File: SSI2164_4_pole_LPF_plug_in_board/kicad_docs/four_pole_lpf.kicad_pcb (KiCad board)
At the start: 2 copper layers, 58.4 x 50.8 mm, 83 parts, among them J1 signal_in, J2 CV_in, J3 signal_out, J4 feedback_CV_and_power, Q1 MMBT3904, Q2 MMBT3906, Q3 BCM847DS135, Q4 MMBT3904, Q5 MMBT3904, Q6 MMBT3906, U1 SSM2164, U2 TL072, U3 TL072, U4 TL072, U5 TL072

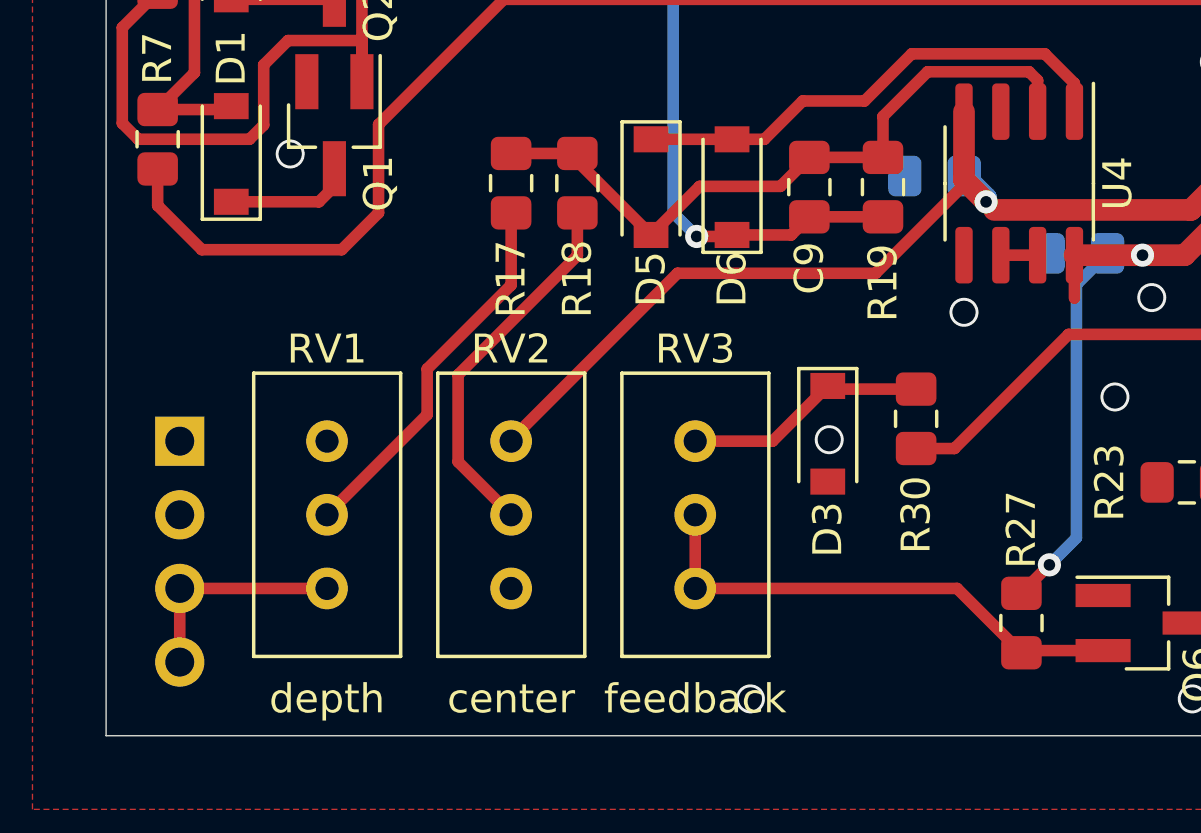
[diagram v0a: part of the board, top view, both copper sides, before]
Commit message: flip trimpots for consistency
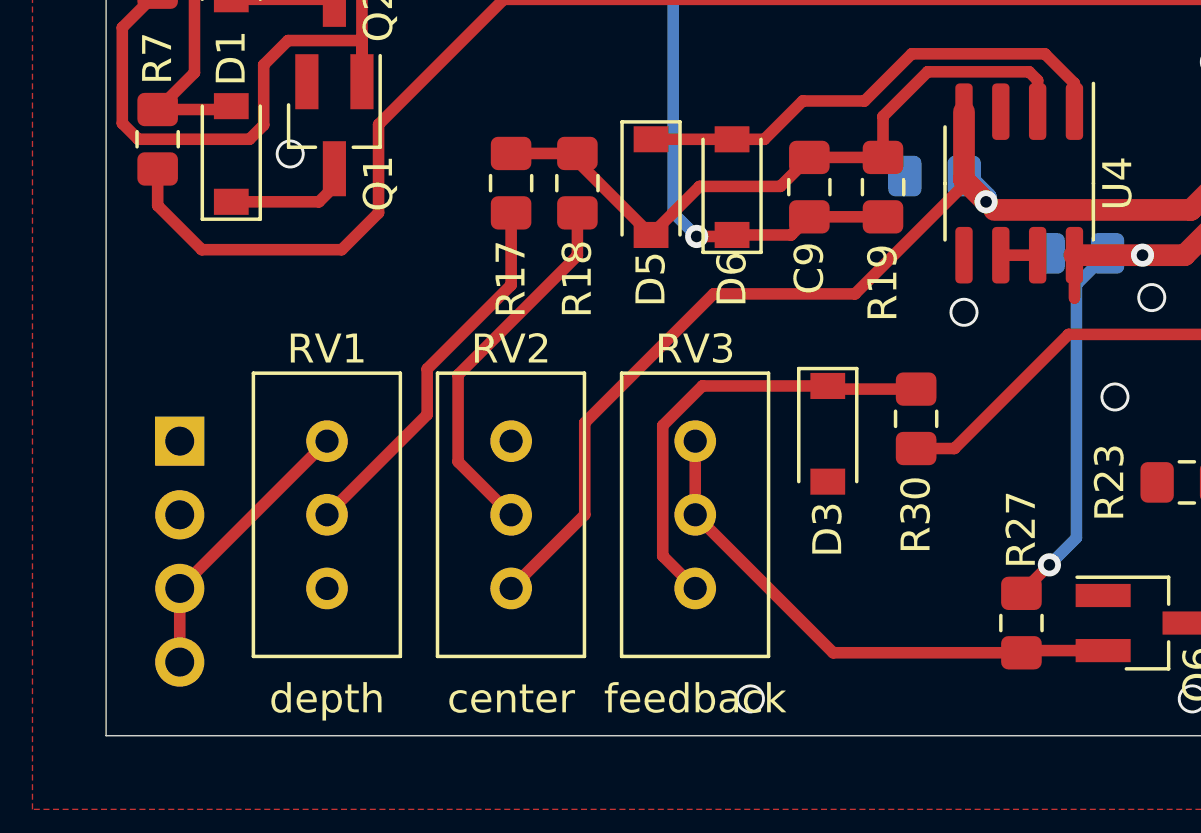
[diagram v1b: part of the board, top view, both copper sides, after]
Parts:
- moved RV1 5.08 mm to (99.1, 111.8), turned to 270 degrees
- moved RV2 5.08 mm to (105.4, 111.8), turned to 270 degrees
- moved RV3 5.08 mm to (111.8, 111.8), turned to 270 degrees
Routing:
- net Net-(D3-Pad1): track 8.45 -> 15.4 mm
- net -12V: track 171.8 -> 175.7 mm
- net /CV_scaler/raw_Vfc_in: track 7.62 -> 9.72 mm
- net Net-(Q6-Pad2): track 17.6 -> 18.6 mm
- net GND: vias 25 -> 24
